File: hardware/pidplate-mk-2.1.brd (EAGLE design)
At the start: 49 x 59 mm, 44 parts, among them J1 M06X2PTH, Q1 2N7000, Q2 2N3904, U1 ATMEGA328P, U3 VSK-S1, Y1 8MHz

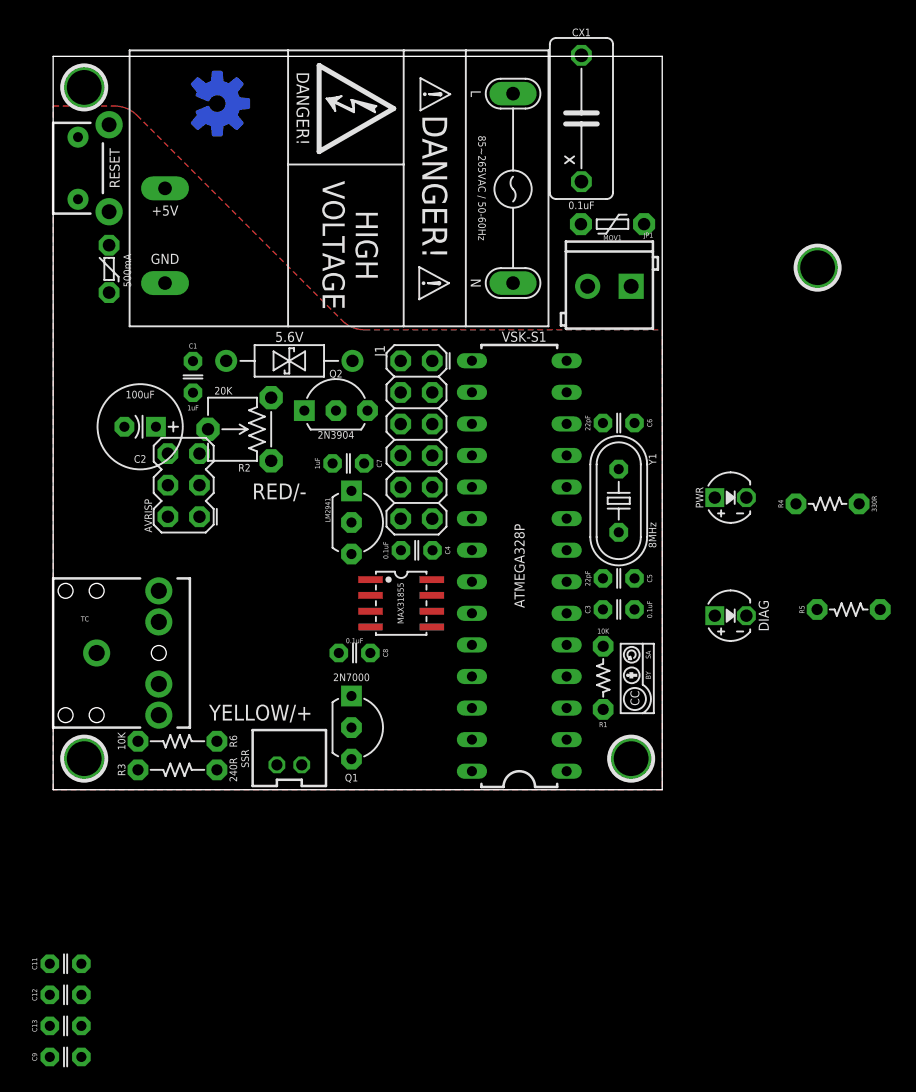
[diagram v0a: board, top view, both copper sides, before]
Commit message: revision dos will use 3.3V power to make life easier
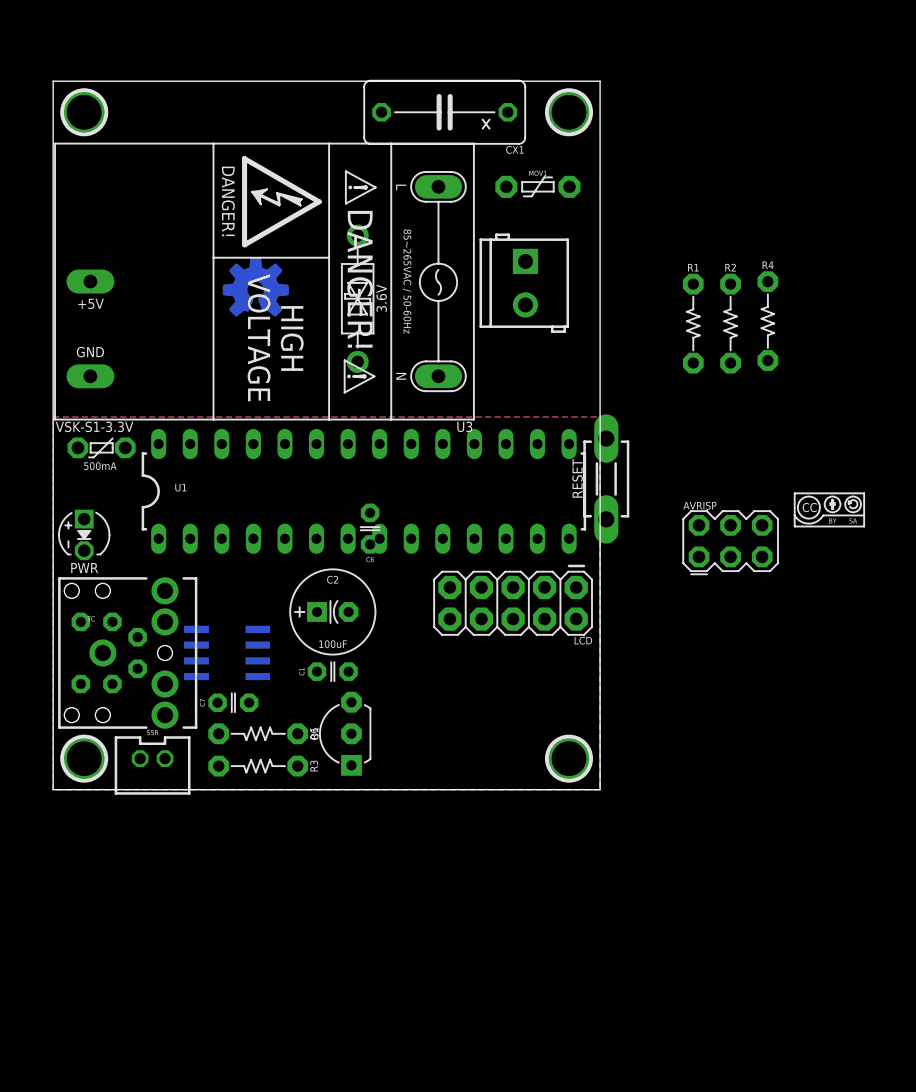
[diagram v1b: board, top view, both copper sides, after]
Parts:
- removed C11, C12, C13, C3, C4: 0.1uF, A_butts:C025-024X044
- removed C5: 22pF, A_butts:C025-024X044
- removed DIAG: LED3MM, A_butts:LED3MM
- removed J1: M06X2PTH, A_butts:2X6_PTH
- removed LM2941: L2941, A_butts:TO-92-AMMO
- removed MAX31855: MAX31855SOIC, A_butts:SOIC127P600X175-8N
- removed Q2: 2N3904, A_butts:TO-92-AMMO
- removed R5: 330R, A_butts:RESISTOR-AXIAL-PTH-5.08MM
- removed Y1: 8MHz, A_butts:HC49U-V
- added C10: 0.1uF, A_butts:C025-024X044
- added LCD: M05X2PTH, A_butts:AVR_ICSP
- added U2: MAX31855, A_butts:SOIC127P600X175-8N
- C6: value 22pF -> 0.1uF
- C7, C9: value 1uF -> 0.1uF
- R1, R4: device A_butts:RESISTOR-AXIAL-PTH-5.08MM -> A_butts:RESISTOR-AXIAL-PTH-6.35MM
- R2: value 20K -> 1k; device A_butts:TRIM_POT_PTH -> A_butts:RESISTOR-AXIAL-PTH-6.35MM
- R3: value 240R -> 120R
- RESET: value SPST-NO-TACT3MM-RA -> SPST-NO-TACT3MM-PTH; device A_butts:TACTILE-PTH-SIDE -> A_butts:DTS-3
- TVS1: value 5.6V -> 3.6V
- U3: value VSK-S1 -> VSK-S1-3.3V
- moved U$3 59.2 mm to (62.7, 28.5), turned to 0 degrees
- moved PWR 52.1 mm to (2.50, 20.5), turned to 270 degrees
- moved RESET 49.3 mm to (44.5, 25.0), turned to 90 degrees
- moved AVRISP 44.2 mm to (54.5, 20.0), turned to 0 degrees
- moved R2 40.4 mm to (54.5, 37.5), turned to 270 degrees
- moved C9 30.1 mm to (3.50, 8.50), flipped to the bottom
- moved R1 29.4 mm to (51.5, 37.5), turned to 270 degrees
- moved C1 26.2 mm to (22.5, 9.50), turned to 0 degrees
- moved H1 23.6 mm to (41.5, 54.5)
- moved C6 21.7 mm to (25.5, 21.0), turned to 90 degrees
- moved C2 21.5 mm to (22.5, 14.3), turned to 0 degrees
- moved C7 21.4 mm to (14.5, 7.00)
- moved C8 20.9 mm to (3.50, 13.5), flipped to the bottom, turned to 0 degrees
- moved U$2 20.8 mm to (60.8, 22.7), turned to 0 degrees
- moved R4 15.5 mm to (57.5, 37.7), turned to 270 degrees
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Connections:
- removed net 5V: AVRISP.2, C1.1, C2.+, C7.1, J1.10, LM2941.1, PTC.P$2, Q2.1, R1.P$2, R2.3, R3.P$1, R4.P$2, TVS1.P$2
- removed net BACKLIGHT: Q2.2, U1.12
- removed net BL-A: J1.4, Q2.3
- removed net CONTRAST: J1.8, R2.2
- removed net DIAG: R5.P$2, U1.11
- removed net N$3: C6.1, U1.10, Y1.1
- removed net N$4: C5.1, U1.9, Y1.2
- removed net N$5: C4.1, U1.21
- removed net RX: U1.2
- removed net TX: U1.3
- net 3.3V: now also AVRISP.2, C1.1, C2.+, C6.1, C7.1, LCD.2, PTC.P$2, R1.P$2, R3.P$1, R4.P$2, TVS1.P$2, U2.4; no longer C3.1, C8.1, C9.1, LM2941.3, MAX31855.4
- net AC(L): now also JP1.1; no longer JP1.2
- net AC(N): now also JP1.2; no longer JP1.1
- net DB4: now also LCD.7; no longer J1.1
- net DB5: now also LCD.8; no longer J1.3
- net DB6: now also LCD.9; no longer J1.5
- net DB7: now also LCD.10; no longer J1.7
- net E: now also LCD.6; no longer J1.2
- net GND: now also LCD.1, R2.P$1, U1.21, U2.1; no longer C11.2, C12.2, C3.2, C4.2, C5.2, DIAG.K, J1.12, J1.6, LM2941.2, MAX31855.1, R2.1
- net N$2: now also LCD.3, R2.P$2; no longer DIAG.A, R5.P$1
- net RS: now also LCD.4; no longer J1.9
- net RW: now also LCD.5; no longer J1.11
- net TC+/YELLOW: now also C10.1, C8.1, TC.RING, U2.3; no longer C11.1, C13.1, MAX31855.3, TC.TIP
- net TC-/RED: now also C10.2, C9.1, TC.TIP, U2.2; no longer C12.1, C13.2, MAX31855.2, TC.RING
- net TC_CLK: now also U2.5; no longer MAX31855.5
- net TC_CS: now also U2.6; no longer MAX31855.6
- net TC_DATA: now also U2.7; no longer MAX31855.7
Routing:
- added copper zone on layer 16, net GND
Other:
- board size 49 x 59 mm -> 44 x 57 mm
- board text removed: "RED/-"
- board text removed: "YELLOW/+"

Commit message: now 50x50mm, reduced components, relatively happy with layout
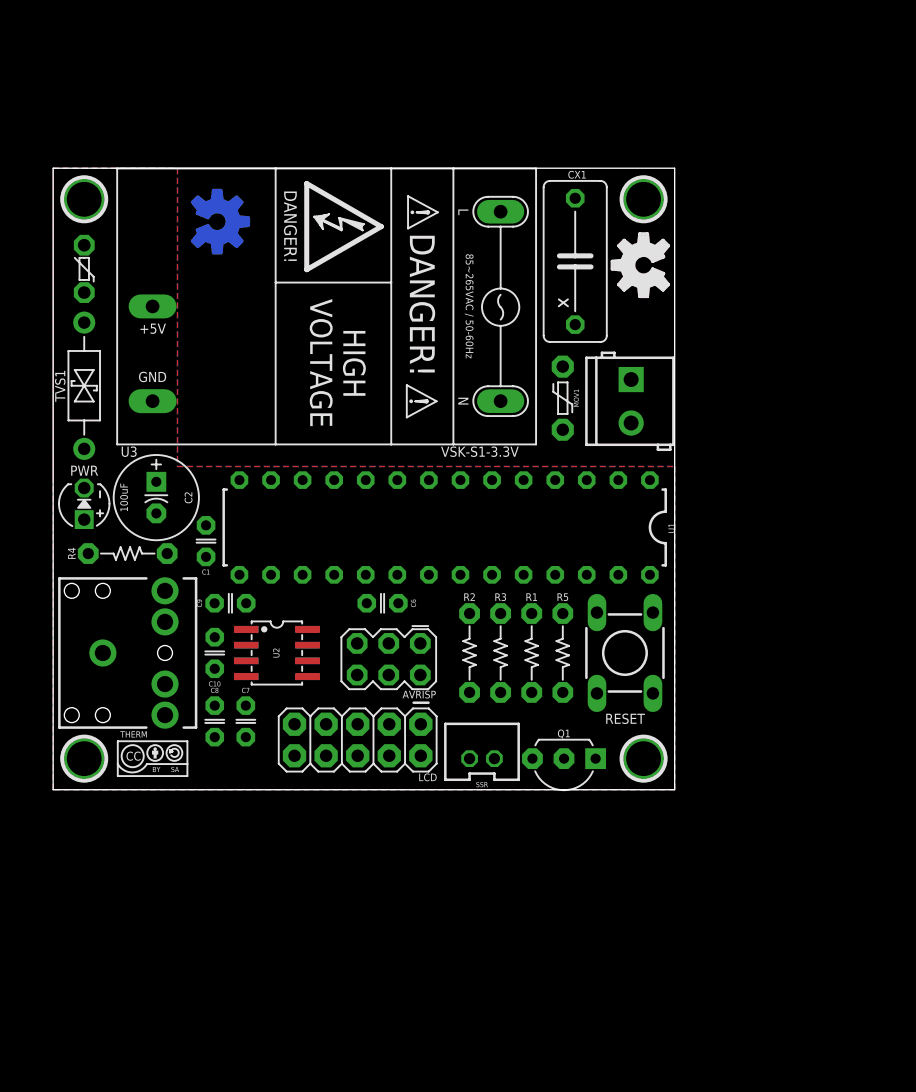
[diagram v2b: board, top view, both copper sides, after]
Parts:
- removed R6: 10K, A_butts:RESISTOR-AXIAL-PTH-6.35MM
- added R5: 10K, A_butts:RESISTOR-AXIAL-PTH-6.35MM
- added U$1: (no value), A_butts:OSHWLOGO_BOT_0.2
- RESET: value SPST-NO-TACT3MM-PTH -> SPST-NO-TACT6MM-PTH; device A_butts:DTS-3 -> A_butts:DTS-6
- U$3: device A_butts:CC-BY-SA-4.0-URL-BOTTOM -> A_butts:CC-BY-SA-4.0-NO-URL
- moved U$2 56.5 mm to (8.00, 2.50)
- moved R4 54.8 mm to (6.00, 19.0), turned to 0 degrees
- moved U$3 50.8 mm to (13.0, 39.0), turned to 90 degrees
- moved R2 33.8 mm to (33.5, 11.0)
- moved R1 29.5 mm to (38.5, 11.0)
- moved AVRISP 29.1 mm to (27.0, 10.5), turned to 180 degrees
- moved SSR 26.5 mm to (34.5, 2.50), turned to 0 degrees
- moved TVS1 23.1 mm to (2.50, 32.5), turned to 90 degrees
- moved R3 21.5 mm to (36.0, 11.0), turned to 270 degrees
- moved Q1 17.2 mm to (41.1, 2.50), turned to 180 degrees
- moved MOV1 17.1 mm to (41.0, 31.5), turned to 270 degrees
- moved C2 16.9 mm to (8.30, 23.5), turned to 270 degrees
- moved LCD 16.7 mm to (24.5, 4.00)
- moved CX1 15.9 mm to (42.0, 42.5), turned to 90 degrees
- moved C1 14.6 mm to (12.3, 20.0), turned to 90 degrees
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- renumbered TC to THERM
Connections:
- net AC(L): now also JP1.2; no longer JP1.1
- net AC(N): now also JP1.1; no longer JP1.2
- net GND: now also R5.P$1, RESET.2; no longer R6.P$2
- net RESET: now also RESET.3, RESET.4; no longer RESET.2
- net SSR: now also R5.P$2; no longer R6.P$1
- net TC+/YELLOW: now also THERM.TIP; no longer THERM.RING
- net TC-/RED: now also THERM.RING; no longer THERM.TIP
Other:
- board size 44 x 57 mm -> 50 x 50 mm

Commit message: mini mini mini
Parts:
- RESET: value SPST-NO-TACT6MM-PTH -> SPST-NO-TACT3MM-PTH-SMALL-PADS; device A_butts:DTS-6 -> A_butts:DTS-3-SMALL-PADS
- THERM: device A_butts:AUDIO-JACK -> A_butts:STEREOJACK2.5MM_STEREOJACK2.5MM
- moved U$2 39.7 mm to (46.0, 14.0)
- moved AVRISP 26.6 mm to (3.00, 22.0), turned to 270 degrees
- moved C1 14.1 mm to (25.5, 15.0), turned to 0 degrees
- moved SSR 13.9 mm to (47.0, 8.50), turned to 90 degrees
- moved RESET 10.3 mm to (39.0, 3.50), turned to 180 degrees
- moved C6 8.08 mm to (18.4, 15.0)
- moved PWR 7.00 mm to (2.50, 16.0)
- moved Q1 6.60 mm to (41.0, 9.10), turned to 270 degrees
- moved R4 6.19 mm to (10.5, 14.8)
- moved R1 6.02 mm to (32.5, 11.5)
- moved R5 6.02 mm to (35.0, 11.5)
- moved C10 4.03 mm to (11.0, 7.50)
- moved U2 4.03 mm to (16.0, 7.50)
- moved C9 4.03 mm to (12.3, 11.5)
- moved C8 3.83 mm to (9.73, 3.50), turned to 180 degrees
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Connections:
- net 3.3V: now also R1.P$1; no longer R1.P$2
- net GND: now also R5.P$2, THERM.SHIELD; no longer R5.P$1, RESET.2, THERM.SLEEVE
- net N$6: now also SSR.2; no longer SSR.1
- net N$9: now also SSR.1; no longer SSR.2
- net RESET: now also R1.P$2, RESET.2; no longer R1.P$1, RESET.3, RESET.4
- net SSR: now also R5.P$1; no longer R5.P$2
- net TC+/YELLOW: now also THERM.RING1, THERM.RING2; no longer THERM.TIP
- net TC-/RED: now also THERM.TIP; no longer THERM.RING

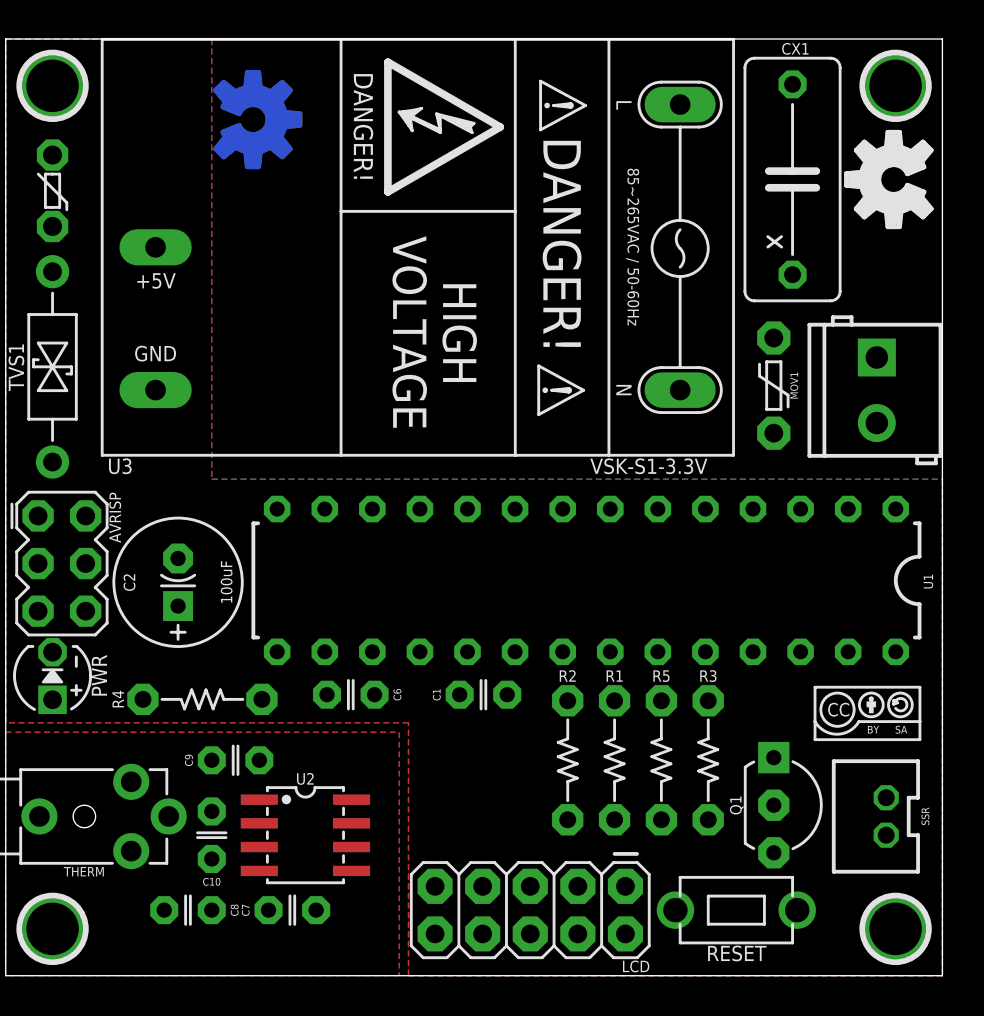
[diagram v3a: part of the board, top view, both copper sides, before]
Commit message: more tweaks to standalone; new shield-based version
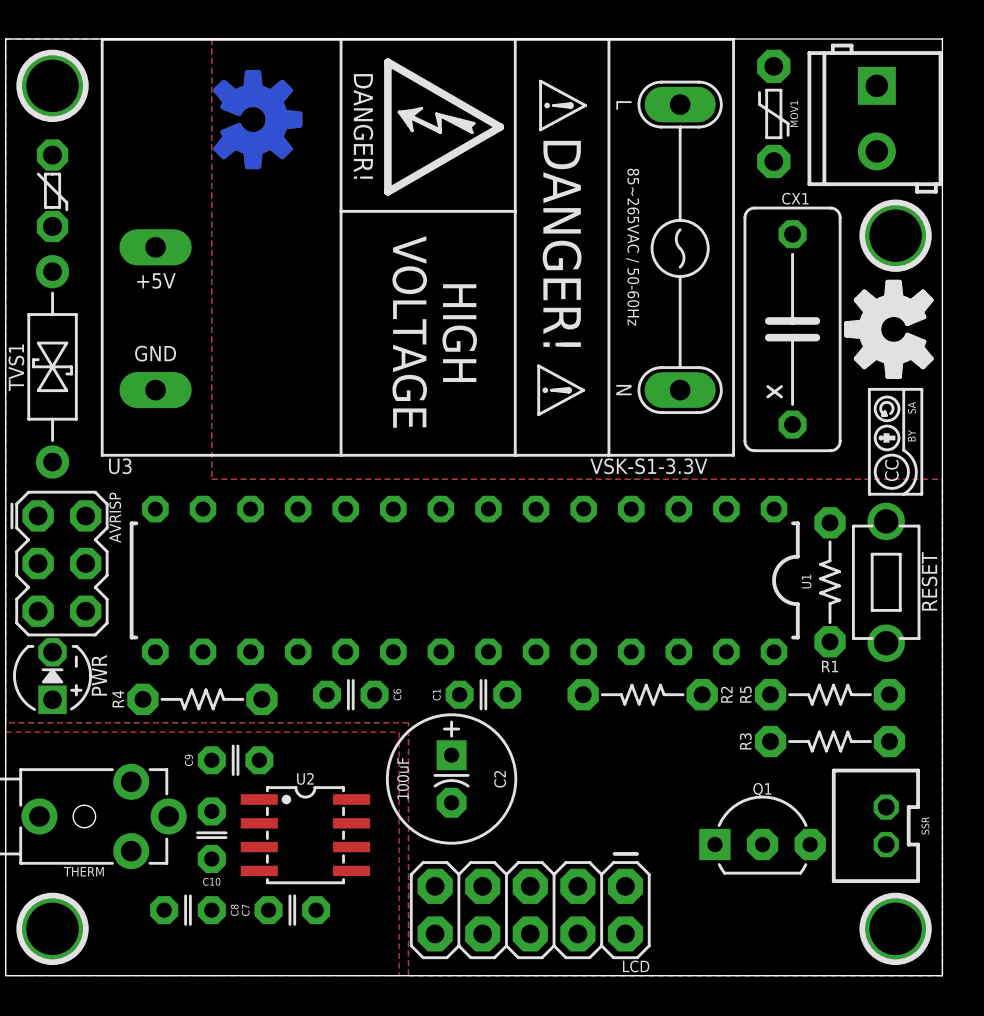
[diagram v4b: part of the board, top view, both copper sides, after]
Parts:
- moved RESET 19.2 mm to (47.0, 21.0), turned to 270 degrees
- moved C2 18.0 mm to (23.8, 10.5), turned to 270 degrees
- moved R1 14.9 mm to (44.0, 21.0), turned to 90 degrees
- moved U$2 14.6 mm to (47.5, 28.5), turned to 90 degrees
- moved JP1 14.5 mm to (46.5, 47.5)
- moved MOV1 14.5 mm to (41.0, 46.0)
- moved R5 9.66 mm to (44.0, 15.0), turned to 0 degrees
- moved CX1 8.00 mm to (42.0, 34.5)
- moved H1 8.00 mm to (47.5, 39.5)
- moved U$1 8.00 mm to (47.4, 34.5)
- moved R3 6.58 mm to (44.0, 12.5), turned to 0 degrees
- moved U1 6.50 mm to (24.5, 21.1)
- moved R2 5.32 mm to (34.0, 15.0), turned to 180 degrees
- moved Q1 2.18 mm to (40.4, 7.00), turned to 0 degrees
- moved SSR 0.50 mm to (47.0, 8.00)
